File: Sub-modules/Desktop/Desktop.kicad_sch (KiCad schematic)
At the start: 41 parts, among them J1 USB_C_Receptacle_USB2.0_14P, J3 PR5L5015-5P-C-H, J4 PR5L5015-5P-C-H, SW2 SKRPACE010, SW3 SKRPACE010, U1 RP2040, U2 W25Q16JVSS, U3 AT24CS02-SSHM, U4 TLV75733PDBV, U5 AHT20, U6 MAX40200AUK, U7 MCP79410, Y1 ABM8-272-T3, Y2 X1A0000610006

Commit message: Added new Desktop submodule
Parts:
- removed R21, R22: 4k7, PCM_Resistor_SMD_AKL:R_0402_1005Metric, symbol Device:R_Small
- removed U5: AHT20, AHT20:PSON100P300X300X110-6N, symbol Desktop Library:AHT20
- added C11, C12, C16, C17, C19, C20, C9: 0u1, Capacitor_SMD:C_0402_1005Metric, symbol Device:C_Small
- added C21, C4: 1u, Capacitor_SMD:C_0402_1005Metric, symbol Device:C_Small
- added C3: 4n7, Capacitor_SMD:C_0402_1005Metric, symbol Device:C_Small
- added D2: SK9822-EC20, PCM_SparkFun-LED:APA102_2020-6Pin, symbol PCM_SparkFun-LED:APA102_2020-6Pin
- added R1, R7, R8: 4k7, PCM_Resistor_SMD_AKL:R_0402_1005Metric, symbol Device:R_Small
- added R3: 1M, PCM_Resistor_SMD_AKL:R_0402_1005Metric, symbol Device:R_Small
- added SW2: SW_Push, PCM_Switch_Keyboard_Hotswap_Kailh:SW_Hotswap_Kailh_MX, symbol Switch:SW_Push
- added U5: STCC4, PCM_SparkFun-Sensor:STCC4, symbol PCM_SparkFun-Sensor:STCC4
- added U6: STHS34PF80, STHS34PF80TR:XDCR_STHS34PF80TR, symbol Desktop Library:STHS34PF80
- added U7: VEML7700-TT, PCM_SparkFun-Sensor:VEML7700-TT, symbol PCM_SparkFun-Sensor:VEML7700-TT
- added U9: SHT40, Sensor_Humidity:Sensirion_DFN-4_1.5x1.5mm_P0.8mm_SHT4x_NoCentralPad, symbol PCM_SparkFun-Sensor:SHT40
- BT1: footprint (none) -> Battery:BatteryHolder_Keystone_1060_1x2032
- C10: renamed from C4; KiLib_Generator (none) -> SMD_2terminal_chip_molded
- C13: renamed from C9; footprint (none) -> Capacitor_SMD:C_0402_1005Metric; KiLib_Generator (none) -> SMD_2terminal_chip_molded
- C14: renamed from C10; footprint (none) -> Capacitor_SMD:C_0402_1005Metric; KiLib_Generator (none) -> SMD_2terminal_chip_molded
- C15: renamed from C11; footprint (none) -> Capacitor_SMD:C_0402_1005Metric; KiLib_Generator (none) -> SMD_2terminal_chip_molded
- C18: renamed from C2; footprint (none) -> Capacitor_SMD:C_0402_1005Metric; KiLib_Generator (none) -> SMD_2terminal_chip_molded
- C2: renamed from C1; footprint (none) -> Capacitor_SMD:C_0402_1005Metric; KiLib_Generator (none) -> SMD_2terminal_chip_molded
- C6: footprint (none) -> Capacitor_SMD:C_0402_1005Metric; KiLib_Generator (none) -> SMD_2terminal_chip_molded
- C7: renamed from C5; footprint (none) -> Capacitor_SMD:C_0402_1005Metric; KiLib_Generator (none) -> SMD_2terminal_chip_molded
- C8: renamed from C3; KiLib_Generator (none) -> SMD_2terminal_chip_molded
- J1: footprint (none) -> Connector_USB:USB_C_Receptacle_HCTL_HC-TYPE-C-16P-01A
- J2: renamed from J3; KiLib_Generator (none) -> connector/pin_header_socket
- J3: renamed from J4; KiLib_Generator (none) -> connector/pin_header_socket
- R13: renamed from R1; footprint (none) -> PCM_Resistor_SMD_AKL:R_0402_1005Metric
- R6: renamed from R2; footprint (none) -> PCM_Resistor_SMD_AKL:R_0402_1005Metric
- U1: renamed from U2; KiLib_Generator (none) -> package/gullwing
- U10: renamed from U3; KiLib_Generator (none) -> package/gullwing
- U3: renamed from U1; KiLib_Generator (none) -> package/no_lead; private KLC_S4.2_VREG_VOUT -> (none)
- U4: footprint Package_DFN_QFN:TQFN-16-1EP_3x3mm_P0.5mm_EP1.23x1.23mm -> Package_TO_SOT_SMD:SOT-23-5; KiLib_Generator (none) -> package/gullwing
- U8: renamed from U7; KiLib_Generator (none) -> package/gullwing
- Y1: footprint (none) -> PCM_Crystal_AKL:Crystal_SMD_3225-4Pin_3.2x2.5mm; private KLC_S4.1 -> (none)
- Y2: footprint (none) -> PCM_Crystal_AKL:Crystal_SMD_2012-2Pin_2.0x1.2mm
- renumbered C7 to C1, C8 to C5, D5 to D3, D7 to D4, D8 to D5, R18 to R10, R19 to R11, R20 to R12, R3 to R2, R5 to R4, R6 to R5, R17 to R9, SW2 to SW1, U6 to U2
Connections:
- net VDD is gone; now on net VBUS: C18.1, C8.1, D3.1 (K), U10.8 (VCC), U2.5 (OUT), U4.1 (IN)
- net +1V1: now also C21.1
- net +3V3: now also C11.2, C12.2, C16.2, C17.2, C19.1, C20.1, C9.1, D2.5 (VDD), R1.2, R7.2, R8.2, U5.6 (VDD_IO), U5.7 (VDD), U6.3 (CS), U6.6 (VDD), U6.9 (VDD), U7.2 (VDD), U9.3 (VDD)
- net GND: now also J1.A1 (GND), J1.A12 (GND), J1.B1 (GND), J1.B12 (GND), C11.1, C12.1, C16.1, C17.1, C19.2, C20.2, C21.2, C3.1, C4.2, C9.2, D2.2 (VSS), R3.2, SW2.1, U5.3 (ADDR), U5.4 (GND), U6.2 (RES), U6.7 (GND), U6.8 (GND), U7.3 (GND), U9.4 (VSS)
- net RP_I2C_SCL: now also U3.15 (GPIO12), R8.1, U5.1 (SCL), U6.1 (SCL/SPC), U7.1 (SCL); no longer U3.7 (GPIO5)
- net RP_I2C_SDA: now also U3.14 (GPIO11), R7.1, U5.5 (SDA), U6.4 (SDA/SDIO), U7.4 (SDA); no longer U3.6 (GPIO4)
- net RTC_MFP: now also U3.29 (GPIO18)
- net SNOOZE: now also U3.2 (GPIO0), C4.1, R1.1, SW2.2
- net SUB_I2C_SCL: now also R12.1; no longer R11.1
- net SUB_I2C_SDA: now also R11.1; no longer R12.1
- net SUB_ISCL_C: now also D5.4 (L2); no longer D5.6 (L1)
- net SUB_ISDA_C: now also D5.6 (L1); no longer D5.4 (L2)
- net SUB_UART_RXD: now also R10.1, U3.40 (GPIO28/ADC2); no longer R9.1
- net SUB_UART_TXD: now also R9.1, U3.41 (GPIO29/ADC3); no longer R10.1
- net SUB_URXD_C: now also D4.4 (L2); no longer D4.6 (L1)
- net SUB_UTXD_C: now also D4.6 (L1); no longer D4.4 (L2)
- net at J1.SH (SHIELD): now also C3.2, R3.1
- net RGB_CLK: now reaches U3.36 (GPIO24)
- net RGB_CLK: now also D2.4 (CI)
- net RGB_DATA: now reaches U3.37 (GPIO25)
- net RGB_DATA: now also D2.3 (DI)
- net PS_INT: now reaches U3.9 (GPIO7)
- net PS_INT: now also U6.10 (INT)
- new net: U5.2 (SDA_C), U9.1 (SDA)
- new net: U5.8 (SCL_C), U9.2 (SCL)
- no-connect marks 4 -> 23
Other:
- note added: "0x10"
- note added: "0x50"
- note added: "0x5A"
- note added: "0x64"
- note added: "0x6F"
- note added: "Ambient Light Sensor"
- note added: "Combined CO2, Relative Humidity and Temperature Sensing"
- note added: "IR Presence Sensor"
- note added: "Real-Time Clock"

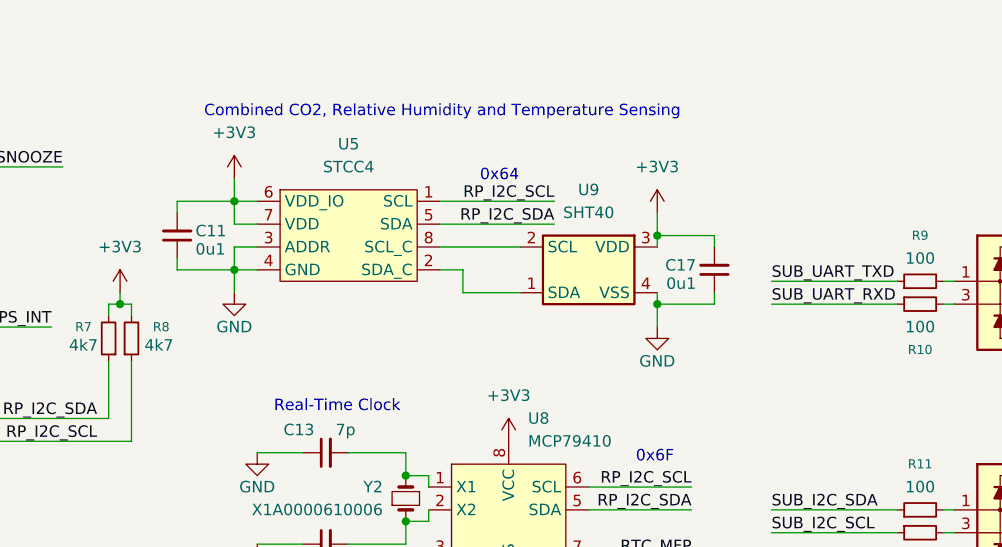
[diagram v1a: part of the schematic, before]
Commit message: Desktop v1.1: changed CO2 sensor to SCD40 changed location and orientation of presence sensor
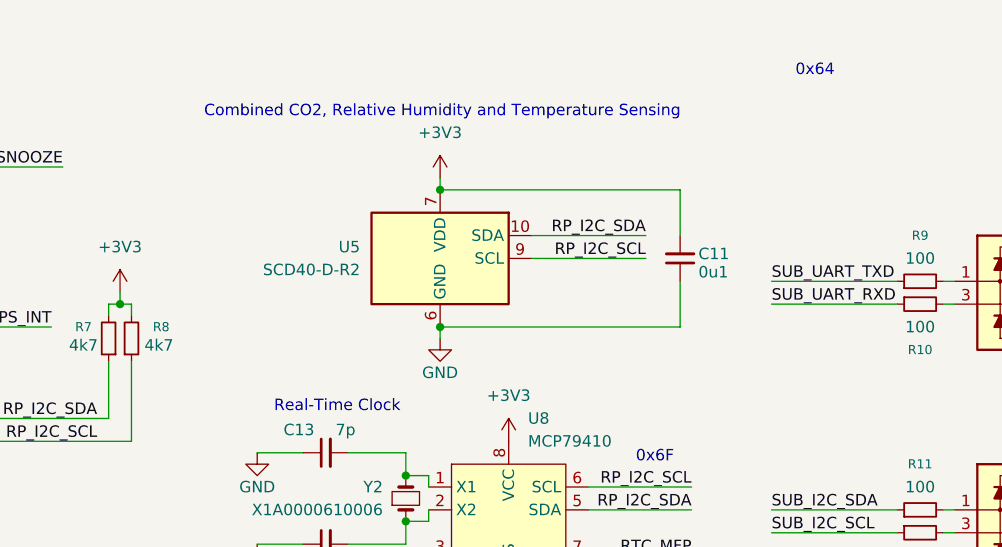
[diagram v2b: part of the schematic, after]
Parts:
- removed C17: 0u1, Capacitor_SMD:C_0402_1005Metric, symbol Device:C_Small
- removed U5: STCC4, PCM_SparkFun-Sensor:STCC4, symbol PCM_SparkFun-Sensor:STCC4
- removed U9: SHT40, Sensor_Humidity:Sensirion_DFN-4_1.5x1.5mm_P0.8mm_SHT4x_NoCentralPad, symbol PCM_SparkFun-Sensor:SHT40
- added U5: SCD40-D-R2, Sensor:Sensirion_SCD4x-1EP_10.1x10.1mm_P1.25mm_EP4.8x4.8mm, symbol Sensor_Gas:SCD40-D-R2
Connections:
- net +3V3: now also U5.19 (VDD), U5.7 (VDD)
- net GND: now also U5.20 (GND), U5.21 (GND), U5.6 (GND)
- net RP_I2C_SCL: now also U5.9 (SCL)
- net RP_I2C_SDA: now also U5.10 (SDA)

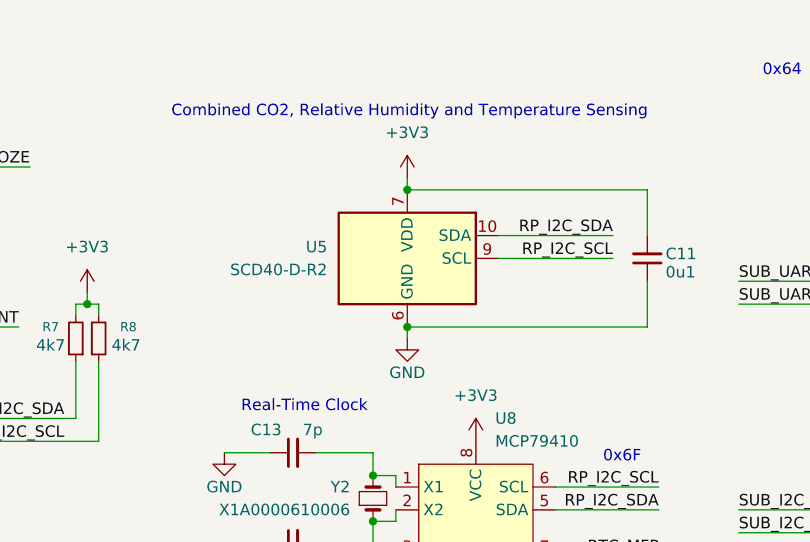
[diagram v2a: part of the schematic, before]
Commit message: Desktop v1.15: revert to SHT40 for cost reduction
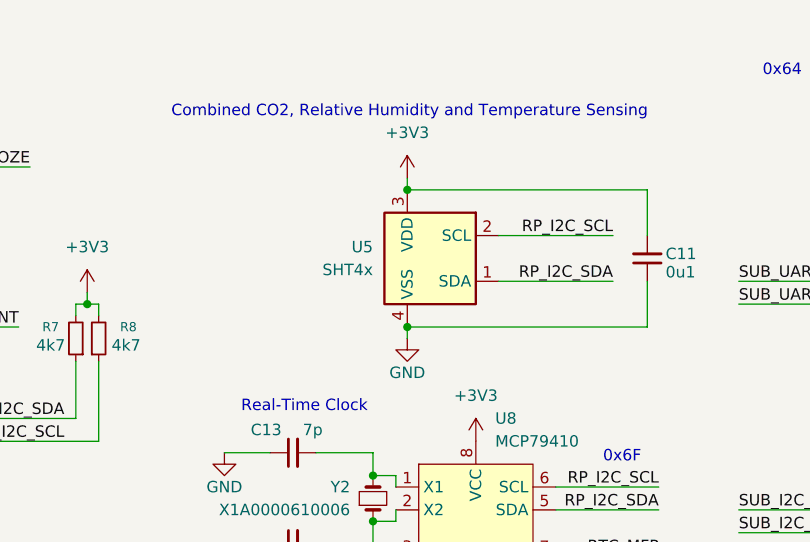
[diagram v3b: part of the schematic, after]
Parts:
- removed U5: SCD40-D-R2, Sensor:Sensirion_SCD4x-1EP_10.1x10.1mm_P1.25mm_EP4.8x4.8mm, symbol Sensor_Gas:SCD40-D-R2
- added U5: SHT4x, Sensor_Humidity:Sensirion_DFN-4_1.5x1.5mm_P0.8mm_SHT4x_NoCentralPad, symbol Sensor_Humidity:SHT4x
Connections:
- net +3V3: now also U5.3 (VDD)
- net GND: now also U5.4 (VSS)
- net RP_I2C_SCL: now also U5.2 (SCL)
- net RP_I2C_SDA: now also U5.1 (SDA)
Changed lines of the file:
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@@
 	)
 	(junction
-		(at 179.07 31.75)
-		(diameter 0)
-		(color 0 0 0 0)
-	)
-	(junction
 		(at 90.17 20.32)
 		(diameter 0)
@@
 	)
 	(junction
+		(at 179.07 31.75)
+		(diameter 0)
+		(color 0 0 0 0)
+	)
+	(junction
 		(at 139.7 162.56)
 		(diameter 0)
@@
 	)
 	(junction
-		(at 179.07 46.99)
-		(diameter 0)
-		(color 0 0 0 0)
-	)
-	(junction
 		(at 110.49 20.32)
 		(diameter 0)
@@
 	)
 	(junction
+		(at 179.07 46.99)
+		(diameter 0)
+		(color 0 0 0 0)
+	)
+	(junction
 		(at 143.51 44.45)
 		(diameter 0)
@@
 	(wire
 		(pts
-			(xy 189.23 39.37) (xy 201.93 39.37)
+			(xy 189.23 41.91) (xy 201.93 41.91)
 		)
 		(stroke
@@
 	)
 	(label "RP_I2C_SDA"
-		(at 201.93 36.83 180)
-		(effects
-			(font
-				(size 1.27 1.27)
-			)
-			(justify right bottom)
-		)
-	)
-	(label "RP_I2C_SDA"
 		(at 198.12 133.35 180)
 		(effects
@@
 		)
 	)
-	(label "RP_I2C_SCL"
-		(at 201.93 39.37 180)
+	(label "SUB_ISDA_C"
+		(at 237.49 109.22 0)
 		(effects
 			(font
 				(size 1.27 1.27)
 			)
-			(justify right bottom)
+			(justify left bottom)
 		)
 	)
-	(label "SUB_ISDA_C"
-		(at 237.49 109.22 0)
+	(label "RP_I2C_SCL"
+		(at 201.93 36.83 180)
 		(effects
 			(font
 				(size 1.27 1.27)
 			)
-			(justify left bottom)
+			(justify right bottom)
 		)
 	)
@@
 		)
 	)
+	(label "RP_I2C_SDA"
+		(at 201.93 41.91 180)
+		(effects
+			(font
+				(size 1.27 1.27)
+			)
+			(justify right bottom)
+		)
+	)
 	(label "RP_I2C_SCL"
 		(at 140.97 59.69 180)
@@
 	)
 	(symbol
-		(lib_id "Sensor_Gas:SCD40-D-R2")
-		(at 179.07 39.37 0)
-		(unit 1)
-		(body_style 1)
-		(exclude_from_sim no)
-		(in_bom yes)
-		(on_board yes)
-		(in_pos_files yes)
-		(dnp no)
-		(fields_autoplaced yes)
-		(property "Reference" "U5"
-			(at 170.18 38.0999 0)
-			(show_name no)
-			(do_not_autoplace no)
-			(effects
-				(font
-					(size 1.27 1.27)
-				)
-				(justify right)
-			)
-		)
-		(property "Value" "SCD40-D-R2"
-			(at 170.18 40.6399 0)
-			(show_name no)
-			(do_not_autoplace no)
-			(effects
-				(font
-					(size 1.27 1.27)
-				)
-				(justify right)
-			)
-		)
-		(property "Footprint" "Sensor:Sensirion_SCD4x-1EP_10.1x10.1mm_P1.25mm_EP4.8x4.8mm"
-			(at 179.07 39.37 0)
-			(hide yes)
-			(show_name no)
-			(do_not_autoplace no)
-			(effects
-				(font
-					(size 1.27 1.27)
-				)
-			)
-		)
-		(property "Datasheet" "https://sensirion.com/media/documents/E0F04247/631EF271/CD_DS_SCD40_SCD41_Datasheet_D1.pdf"
-			(at 179.07 39.37 0)
-			(hide yes)
-			(show_name no)
-			(do_not_autoplace no)
-			(effects
-				(font
-					(size 1.27 1.27)
-				)
-			)
-		)
-		(property "Description" "Photoacoustic CO2 sensor, 40 000 ppm, I2C, 2.4-5.5 V, Base accuracy  400 - 2000 ppm"
-			(at 179.07 39.37 0)
-			(hide yes)
-			(show_name no)
-			(do_not_autoplace no)
-			(effects
-				(font
-					(size 1.27 1.27)
-				)
-			)
-		)
-		(pin "7"
-		)
-		(pin "9"
-		)
-		(pin "10"
-		)
-		(pin "19"
-		)
-		(pin "6"
-		)
-		(pin "20"
-		)
-		(pin "21"
-		)
-		(instances
-			(project "Desktop"
-				(path "/3bd174a1-39fe-431a-9b69-24332a115343"
-					(reference "U5")
-					(unit 1)
-				)
-			)
-		)
-	)
-	(symbol
 		(lib_id "Device:C_Small")
 		(at 53.34 107.95 0)
@@
 					(unit 1)
 				)
+			)
+		)
+	)
+	(symbol
+		(lib_id "Sensor_Humidity:SHT4x")
+		(at 181.61 39.37 0)
+		(mirror y)
+		(unit 1)
+		(body_style 1)
+		(exclude_from_sim no)
+		(in_bom yes)
+		(on_board yes)
+		(in_pos_files yes)
+		(dnp no)
+		(property "Reference" "U5"
+			(at 175.26 38.0999 0)
+			(show_name no)
+			(do_not_autoplace no)
+			(effects
+				(font
+					(size 1.27 1.27)
+				)
+				(justify left)
+			)
+		)
+		(property "Value" "SHT4x"
+			(at 175.26 40.6399 0)
+			(show_name no)
+			(do_not_autoplace no)
+			(effects
+				(font
+					(size 1.27 1.27)
+				)
+				(justify left)
+			)
+		)
+		(property "Footprint" "Sensor_Humidity:Sensirion_DFN-4_1.5x1.5mm_P0.8mm_SHT4x_NoCentralPad"
+			(at 177.8 45.72 0)
+			(hide yes)
+			(show_name no)
+			(do_not_autoplace no)
+			(effects
+				(font
+					(size 1.27 1.27)
+				)
+				(justify left)
+			)
+		)
+		(property "Datasheet" "https://sensirion.com/media/documents/33FD6951/624C4357/Datasheet_SHT4x.pdf"
+			(at 177.8 48.26 0)
+			(hide yes)
+			(show_name no)
+			(do_not_autoplace no)
+			(effects
+				(font
+					(size 1.27 1.27)
+				)
+				(justify left)
+			)
+		)
+		(property "Description" "Digital Humidity and Temperature Sensor, ±1%RH, ±0.1°C, I2C, 1.08-3.6V, 16bit, DFN-4"
+			(at 181.61 39.37 0)
+			(hide yes)
+			(show_name no)
+			(do_not_autoplace no)
+			(effects
+				(font
+					(size 1.27 1.27)
+				)
+			)
+		)
+		(pin "2"
+		)
+		(pin "3"
+		)
+		(pin "4"
+		)
+		(pin "1"
+		)
+		(instances
+			(project "Desktop"
+				(path "/3bd174a1-39fe-431a-9b69-24332a115343"
+					(reference "U5")
+					(unit 1)
+				)

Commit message: added new Keyboard submodule
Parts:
- added C17: 0u1, Capacitor_SMD:C_0402_1005Metric, symbol Device:C_Small
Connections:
- net +3V3: now also C17.2
- net GND: now also C17.1
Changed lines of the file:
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@@
+	)
+	(symbol
+		(lib_id "Device:C_Small")
+		(at 138.43 132.08 0)
+		(mirror x)
+		(unit 1)
+		(body_style 1)
+		(exclude_from_sim no)
+		(in_bom yes)
+		(on_board yes)
+		(in_pos_files yes)
+		(dnp no)
+		(property "Reference" "C17"
+			(at 140.462 131.572 0)
+			(show_name no)
+			(do_not_autoplace no)
+			(effects
+				(font
+					(size 1.27 1.27)
+				)
+				(justify left)
+			)
+		)
+		(property "Value" "0u1"
+			(at 140.462 133.604 0)
+			(show_name no)
+			(do_not_autoplace no)
+			(effects
+				(font
+					(size 1.27 1.27)
+				)
+				(justify left)
+			)
+		)
+		(property "Footprint" "Capacitor_SMD:C_0402_1005Metric"
+			(at 138.43 132.08 0)
+			(hide yes)
+			(show_name no)
+			(do_not_autoplace no)
+			(effects
+				(font
+					(size 1.27 1.27)
+				)
+			)
+		)
+		(property "Datasheet" ""
+			(at 138.43 132.08 0)
+			(hide yes)
+			(show_name no)
+			(do_not_autoplace no)
+			(effects
+				(font
+					(size 1.27 1.27)
+				)
+			)
+		)
+		(property "Description" "Unpolarized capacitor, small symbol"
+			(at 138.43 132.08 0)
+			(hide yes)
+			(show_name no)
+			(do_not_autoplace no)
+			(effects
+				(font
+					(size 1.27 1.27)
+				)
+			)
+		)
+		(property "KiLib_Generator" "SMD_2terminal_chip_molded"
+			(at 138.43 132.08 0)
+			(hide yes)
+			(show_name no)
+			(do_not_autoplace no)
+			(effects
+				(font
+					(size 1.27 1.27)
+				)
+			)
+		)
+		(pin "1"
+		)
+		(pin "2"
+		)
+		(instances
+			(project "Desktop"
+				(path "/3bd174a1-39fe-431a-9b69-24332a115343"
+					(reference "C17")
+					(unit 1)
+				)
+			)
+		)
 	)
 	(symbol
